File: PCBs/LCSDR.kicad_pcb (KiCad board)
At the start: 2 copper layers, 70 x 61 mm, 97 parts, among them J1 MIC, J10 SPK, J12 Conn_01x01, J13 Conn_01x01, J14 Conn_01x01, J15 Conn_01x01, J2 ANT, J3 Calibration, J5 Conn_01x02, J7 Conn_01x10, J8 Jack-DC, J9 Conn_01x02, K1 TIANBO-HJR-4102-L, Q1 2N7002, Q2 2N7002, Q3 BFR93A, Q4 BS170, Q6 BS170, Q7 BF998, Q8 BS170, Q9 BC849, U1 24LC01, U2 Si5351, U3 L7805, U5 LM1117-3.3, U6 Arduino_Nano, U7 74ACT00, Y1 25Mhz

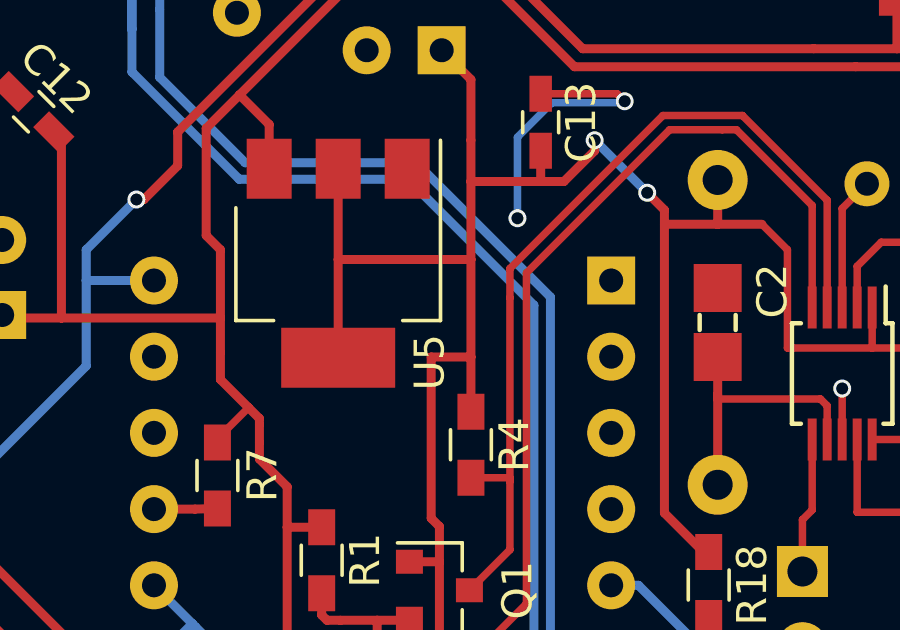
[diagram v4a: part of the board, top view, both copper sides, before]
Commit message: Arduino Nano PCB ADX988 DSP
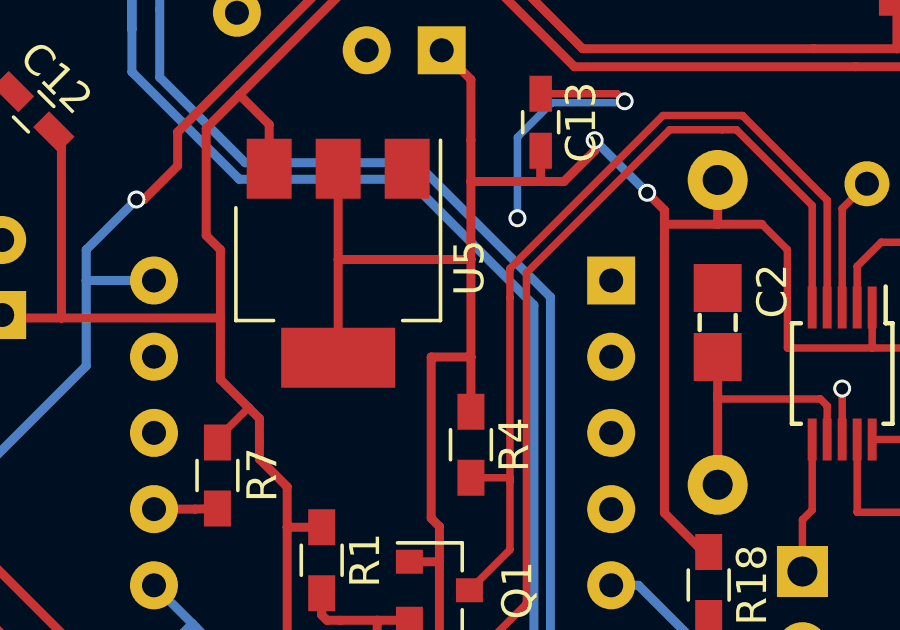
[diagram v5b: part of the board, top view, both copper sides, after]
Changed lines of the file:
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@@
     (tags "CMS SOT")
     (attr smd)
-    (fp_text reference U5 (at 3.3 -3.05 450) (layer F.SilkS)
+    (fp_text reference U5 (at 0.15 -4.375 450) (layer F.SilkS)
       (effects (font (size 1 1) (thickness 0.15)))
     )
@@
   (segment (start 116.1 131.925) (end 117.125 131.925) (width 0.3) (layer F.Cu) (net 4))
   (segment (start 117.125 131.925) (end 117.175 131.875) (width 0.3) (layer F.Cu) (net 4))
-  (segment (start 110.775 126) (end 110.775 125.875) (width 0.25) (layer F.Cu) (net 5) (status C00000))
-  (segment (start 110.775 125.875) (end 111.8125 124.8375) (width 0.25) (layer F.Cu) (net 5) (status 400000))
+  (segment (start 110.775 126) (end 110.775 125.875) (width 0.25) (layer F.Cu) (net 5))
+  (segment (start 110.775 125.875) (end 111.8125 124.8375) (width 0.25) (layer F.Cu) (net 5))
   (segment (start 105.575 121.85) (end 105.575 115.9) (width 0.3) (layer F.Cu) (net 5))
   (segment (start 105.575 115.9) (end 105.321751 115.646751) (width 0.3) (layer F.Cu) (net 5))

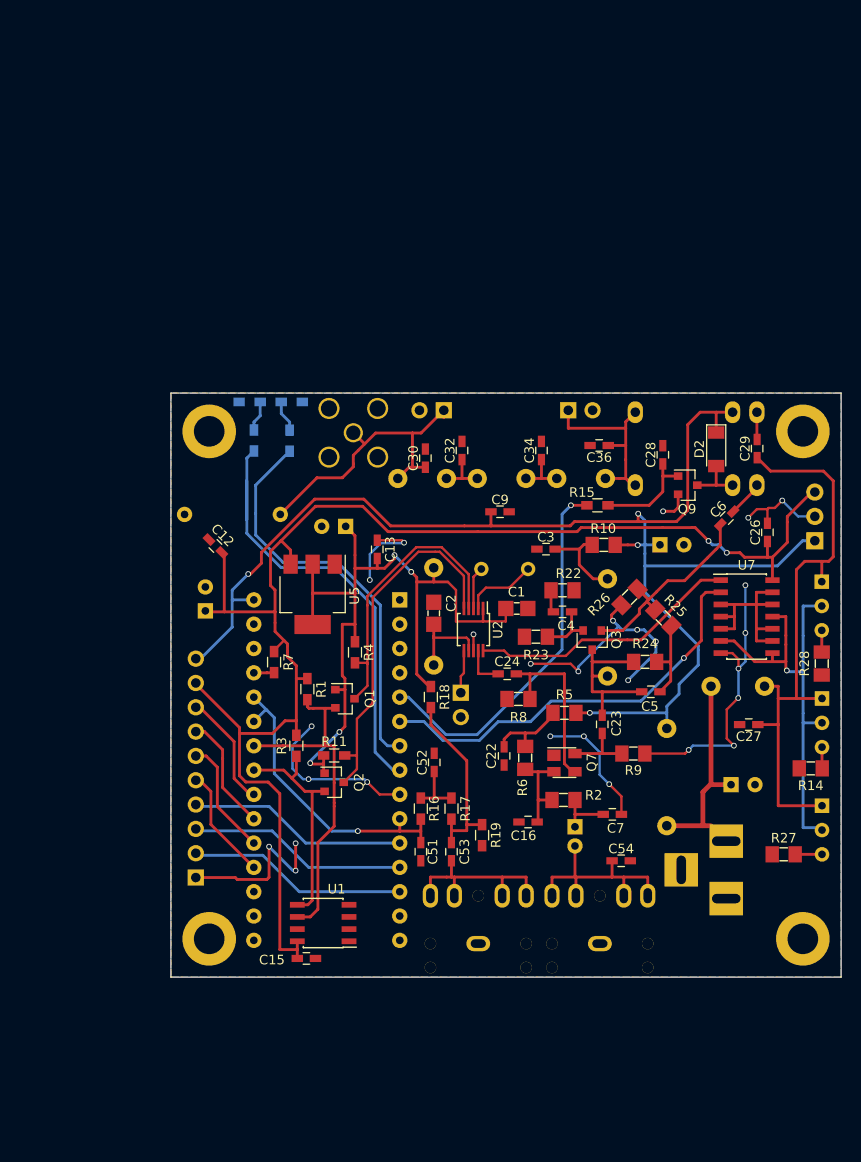
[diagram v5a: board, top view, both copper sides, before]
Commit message: migrate to attiny1614
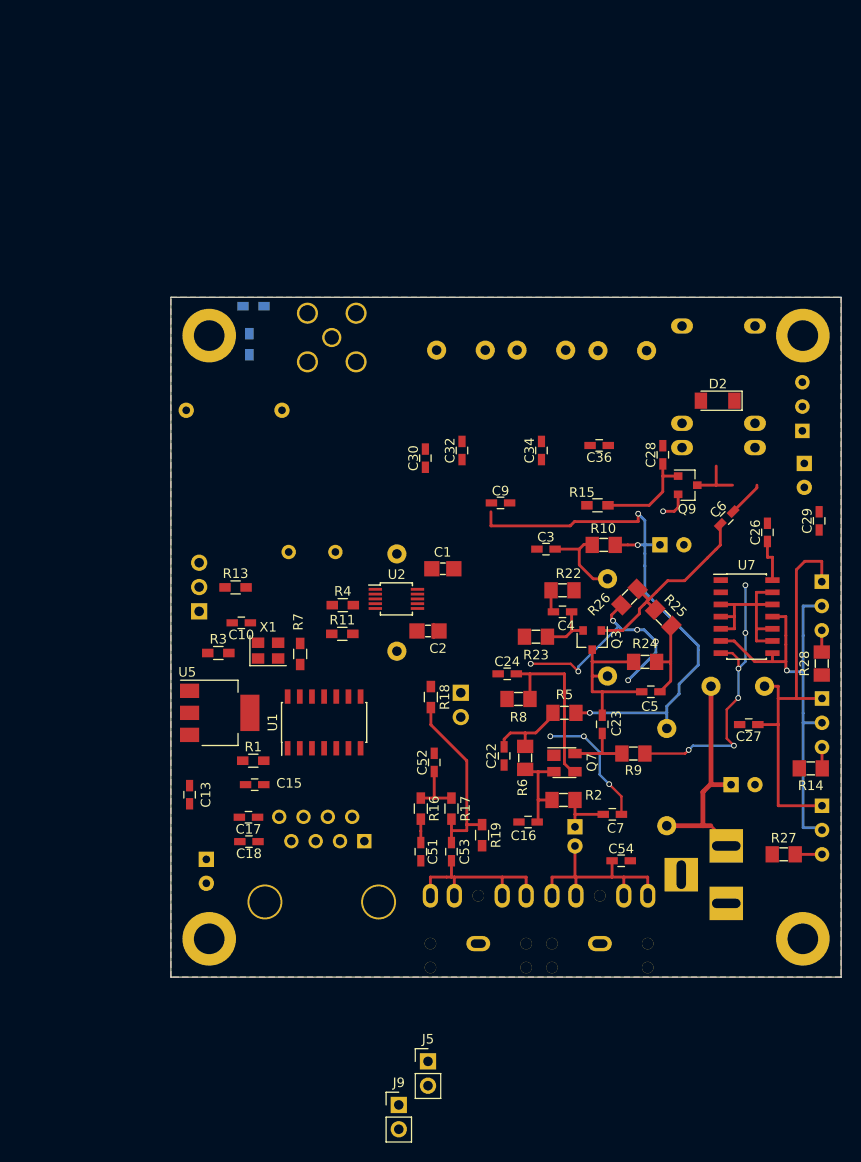
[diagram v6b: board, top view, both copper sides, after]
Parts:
- removed D4: LED, LEDs:LED_0603_HandSoldering
- removed J7: Conn_01x10, Pin_Headers:Pin_Header_Straight_1x10_Pitch2.54mm
- removed Q1, Q2: 2N7002, TO_SOT_Packages_SMD:SOT-23
- removed U6: Arduino_Nano, Arduino:Arduino_Nano
- added C17: 100nF, Capacitors_SMD:C_0603_HandSoldering, F.Cu at (108.1, 143.3)
- added C18: 100nF, Capacitors_SMD:C_0603_HandSoldering, F.Cu at (108.2, 145.8)
- added J4: RJ45, Connectors:RJ45_8, B.Cu at (120.2, 145.8)
- added J6: Conn_01x03, Pin_Headers:Pin_Header_Straight_1x03_Pitch2.54mm, B.Cu at (103.0, 121.8)
- added X1: TXC-7C, Oscillators:Oscillator_SMD_Abracon_ASE-4pin_3.2x2.5mm, F.Cu at (110.2, 125.9)
- C10: value 100uF -> 100nF; footprint Capacitors_THT:CP_Radial_D6.3mm_P2.50mm -> Capacitors_SMD:C_0603_HandSoldering; moved to F.Cu
- C12: value 100nF -> 100uF; footprint Capacitors_SMD:C_0603_HandSoldering -> Capacitors_THT:CP_Radial_D6.3mm_P2.50mm; moved to B.Cu
- J5, J9: moved to F.Cu
- R1: value 10K -> 0
- R13: value 1k -> 47; moved to F.Cu
- R3: value 10K -> 47
- R7: value 0 -> 47
- U1: value 24LC01 -> ATtiny1614-SS; footprint Housings_SOIC:SOIC-8_3.9x4.9mm_Pitch1.27mm -> Housings_SOIC:SOIC-14_3.9x8.7mm_Pitch1.27mm
- U3: value L7805 -> L78L05_TO92; footprint TO_SOT_Packages_THT:TO-220-3_Vertical -> TO_SOT_Packages_THT:TO-92_Inline_Wide
- moved J9 74.7 mm to (123.8, 173.3), turned to 0 degrees
- moved J5 68.0 mm to (126.8, 168.8), turned to 0 degrees
- moved C12 62.1 mm to (166.2, 106.3), turned to 270 degrees
- moved C11 37.7 mm to (103.7, 147.7), turned to 270 degrees
- moved C13 32.3 mm to (102.0, 140.9), turned to 270 degrees
- moved U1 21.0 mm to (116.0, 133.4), turned to 90 degrees
- moved Y1 20.2 mm to (112.3, 115.6)
- moved C15 18.9 mm to (108.8, 139.9), turned to 180 degrees
- moved U5 15.7 mm to (105.1, 132.4), turned to 0 degrees
- moved R13 15.5 mm to (106.8, 119.3), turned to 0 degrees
- moved K1 15.4 mm to (161.0, 92.0), turned to 180 degrees
- moved L8 14.0 mm to (136.2, 99.6)
- moved L10 14.0 mm to (144.6, 99.7)
- moved L6 14.0 mm to (127.8, 99.6)
- moved R11 12.7 mm to (117.9, 124.2)
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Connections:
- C10 pad 1: +5V -> +3V3
- C12 pad 1: +5V -> VCC
- C15 pad 1: +5V -> VCC
- C26 pad 1: +5V -> VCC
- R1 pad 1: +5V -> +3V3
- R1 pad 2: SCL -> VCC
- R11 pad 2: Net-(Q2-Pad3) -> SDA
- R12 pad 1: LED_GREEN -> LED
- R13 pad 1: LED_RED -> Net-(J6-Pad2)
- R13 pad 2: Net-(D4-Pad2) -> RESET_UPDI
- R3 pad 1: +5V -> Net-(J6-Pad1)
- R3 pad 2: SDA -> VCC
- R4 pad 2: Net-(Q1-Pad3) -> SCL
- R7 pad 2: +5V -> Net-(R7-Pad2)
- U1 pad 1: (no net) -> VCC
- U1 pad 3: (no net) -> LED
- U1 pad 4: GND -> AUDIO_IN
- U1 pad 5: SDA -> GND
- U1 pad 6: SCL -> Net-(J4-Pad6)
- U1 pad 7: (no net) -> Net-(J4-Pad3)
- U1 pad 8: +5V -> SDA
- U2 pad 4: Net-(Q1-Pad3) -> SCL
- U2 pad 5: Net-(Q2-Pad3) -> SDA
- U3 pad 1: +12V -> VCC
- U3 pad 3: +5V -> +12V
- U5 pad 3: +5V -> +12V
- U7 pad 14: +5V -> VCC
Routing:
- net +5V: track 152.5 -> 0.00 mm, vias 2 -> 0
- net +12V: track 143.3 -> 58.4 mm, vias 4 -> 3
- net +3V3: track 83.5 -> 0.18 mm, vias 4 -> 0
- net GND: track 128.4 -> 73.1 mm, vias 27 -> 16
- net LED_RED: track 48.0 -> 0.00 mm
- net RX_TX_PA: track 43.4 -> 0.00 mm, vias 1 -> 0
- net LED_GREEN: track 42.6 -> 0.00 mm
- net RX_TX: track 39.4 -> 0.00 mm, vias 1 -> 0
- net Net-(Q2-Pad3): track 37.8 -> 0.00 mm
- net SCL: track 36.3 -> 0.00 mm
- net Net-(C30-Pad1): track 31.7 -> 0.00 mm
- net AUDIO_IN: track 32.9 -> 2.45 mm, vias 1 -> 0
- net Net-(Q1-Pad3): track 30.0 -> 0.00 mm
- net CLK0: track 28.3 -> 0.00 mm
- net SDA: track 24.0 -> 0.00 mm
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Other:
- board size 70 x 61 mm -> 70 x 71 mm
